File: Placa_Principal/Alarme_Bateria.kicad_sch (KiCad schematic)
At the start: 7 parts, among them Q1 BC547, U1 LM358

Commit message: Segundo commit
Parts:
- added R5: 330, Resistor_THT:R_Axial_DIN0204_L3.6mm_D1.6mm_P5.08mm_Horizontal, symbol Device:R_Small_US
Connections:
- net at Q1.2 (B), R1.2: now also R5.2
- new net ESP_GPIO14: R5.1
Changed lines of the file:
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@@
+	)
+	(junction
+		(at 170.18 90.17)
+		(diameter 0)
+		(color 0 0 0 0)
 	)
 	(junction
@@
 	(wire
 		(pts
-			(xy 165.1 90.17) (xy 172.72 90.17)
+			(xy 165.1 90.17) (xy 170.18 90.17)
 		)
 		(stroke
@@
 	(wire
 		(pts
+			(xy 170.18 104.14) (xy 170.18 90.17)
+		)
+		(stroke
+			(width 0)
+			(type default)
+		)
+	)
+	(wire
+		(pts
 			(xy 95.25 88.9) (xy 95.25 92.71)
 		)
@@
 	(wire
 		(pts
+			(xy 165.1 104.14) (xy 170.18 104.14)
+		)
+		(stroke
+			(width 0)
+			(type default)
+		)
+	)
+	(wire
+		(pts
 			(xy 95.25 97.79) (xy 95.25 100.33)
 		)
@@
 	(wire
 		(pts
+			(xy 170.18 90.17) (xy 172.72 90.17)
+		)
+		(stroke
+			(width 0)
+			(type default)
+		)
+	)
+	(wire
+		(pts
 			(xy 170.18 83.82) (xy 170.18 76.2)
 		)
@@
 	(wire
 		(pts
+			(xy 154.94 104.14) (xy 160.02 104.14)
+		)
+		(stroke
+			(width 0)
+			(type default)
+		)
+	)
+	(wire
+		(pts
 			(xy 116.84 88.9) (xy 116.84 92.71)
 		)
@@
 			(width 0)
 			(type default)
+		)
+	)
+	(global_label "ESP_GPIO14"
+		(shape input)
+		(at 154.94 104.14 180)
+		(fields_autoplaced yes)
+		(effects
+			(font
+				(size 1.27 1.27)
+			)
+			(justify right)
+		)
+		(property "Intersheetrefs" "${INTERSHEET_REFS}"
+			(at 140.4644 104.14 0)
+			(effects
+				(font
+					(size 1.27 1.27)
+				)
+				(justify right)
+				(hide yes)
+			)
 		)
 	)
@@
 					(unit 1)
 				)
+			)
+		)
+	)
+	(symbol
+		(lib_id "Device:R_Small_US")
+		(at 162.56 104.14 90)
+		(unit 1)
+		(exclude_from_sim no)
+		(in_bom yes)
+		(on_board yes)
+		(dnp no)
+		(fields_autoplaced yes)
+		(property "Reference" "R5"
+			(at 162.56 97.79 90)
+			(effects
+				(font
+					(size 1.27 1.27)
+				)
+			)
+		)
+		(property "Value" "330"
+			(at 162.56 100.33 90)
+			(effects
+				(font
+					(size 1.27 1.27)
+				)
+			)
+		)
+		(property "Footprint" "Resistor_THT:R_Axial_DIN0204_L3.6mm_D1.6mm_P5.08mm_Horizontal"
+			(at 162.56 104.14 0)
+			(effects
+				(font
+					(size 1.27 1.27)
+				)
+				(hide yes)
+			)
+		)
+		(property "Datasheet" "~"
+			(at 162.56 104.14 0)
+			(effects
+				(font
+					(size 1.27 1.27)
+				)
+				(hide yes)
+			)
+		)
+		(property "Description" "Resistor, small US symbol"
+			(at 162.56 104.14 0)
+			(effects
+				(font
+					(size 1.27 1.27)
+				)
+				(hide yes)
+			)
+		)
+		(pin "2"
+		)
+		(pin "1"
+		)
+		(instances
+			(project "Placa_Principal"
+				(path "/02649df7-f0d0-431b-8f11-0967d1dd03be/fe6eca11-8c4c-4288-9879-38b840f60c23"
+					(reference "R5")
+					(unit 1)
+				)

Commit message: Finalizando o esquemático e rearranjando a posição dos componentes na PCB
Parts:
- R5: value 330 -> ?
- RV1: value R_Potentiometer -> 2k; footprint Potentiometer_THT:Potentiometer_Bourns_3266Y_Vertical -> Custom_Footprints:RTRIM3362P
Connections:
- net ESP_GPIO14 renamed ESP_GPIO00
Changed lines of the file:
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@@
 		)
 	)
-	(global_label "ESP_GPIO14"
+	(global_label "ESP_GPIO00"
 		(shape input)
 		(at 154.94 104.14 180)
@@
 			)
 		)
-		(property "Value" "R_Potentiometer"
+		(property "Value" "2k"
 			(at 130.81 78.74 90)
 			(effects
@@
 			)
 		)
-		(property "Footprint" "Potentiometer_THT:Potentiometer_Bourns_3266Y_Vertical"
+		(property "Footprint" "Custom_Footprints:RTRIM3362P"
 			(at 130.81 82.55 0)
 			(effects
@@
 			)
 		)
-		(property "Value" "330"
+		(property "Value" "?"
 			(at 162.56 100.33 90)
 			(effects

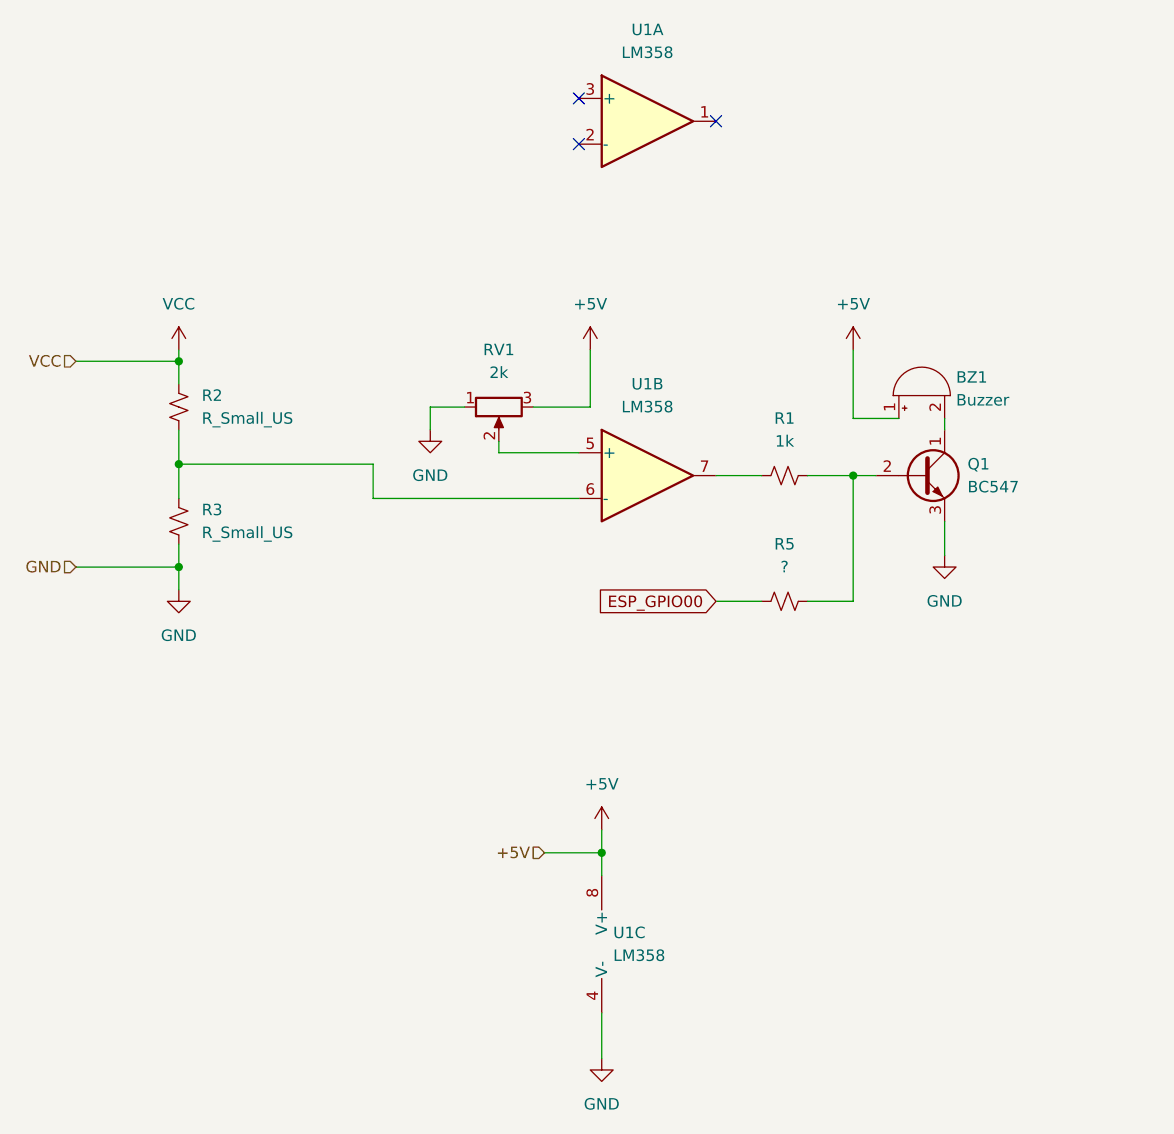
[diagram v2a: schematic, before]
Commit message: Atualizando a alimentação de todos os sensores e ESP para 3.3V e finalizando o design do monitoramento da bateria e feedback geral
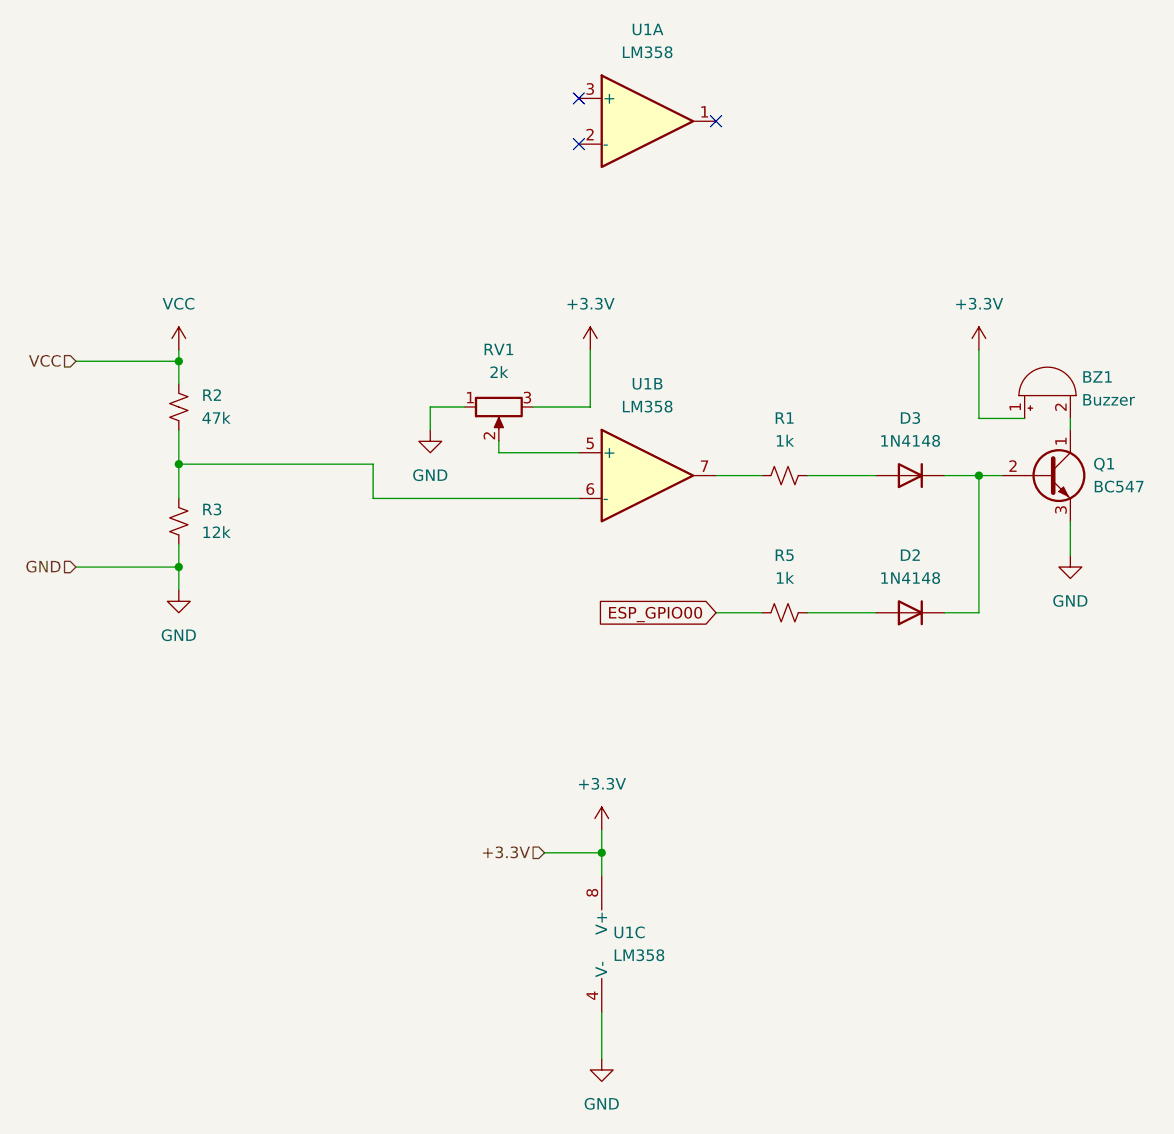
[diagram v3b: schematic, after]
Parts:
- added D2, D3: 1N4148, Diode_THT:D_DO-35_SOD27_P7.62mm_Horizontal, symbol Diode:1N4148
- R2: value R_Small_US -> 47k
- R3: value R_Small_US -> 12k
- R5: value ? -> 1k
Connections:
- net +5V renamed +3.3V
- new net: D2.1 (K), D3.1 (K), Q1.2 (B)
- new net: D3.2 (A), R1.2
- new net: D2.2 (A), R5.2
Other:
- moved on the sheet: BZ1, Q1, R5
